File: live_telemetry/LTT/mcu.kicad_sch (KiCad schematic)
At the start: 15 parts, among them J1 Programming Header, U1 MCP2562, U2 PIC18F26K83, Y1 Crystal

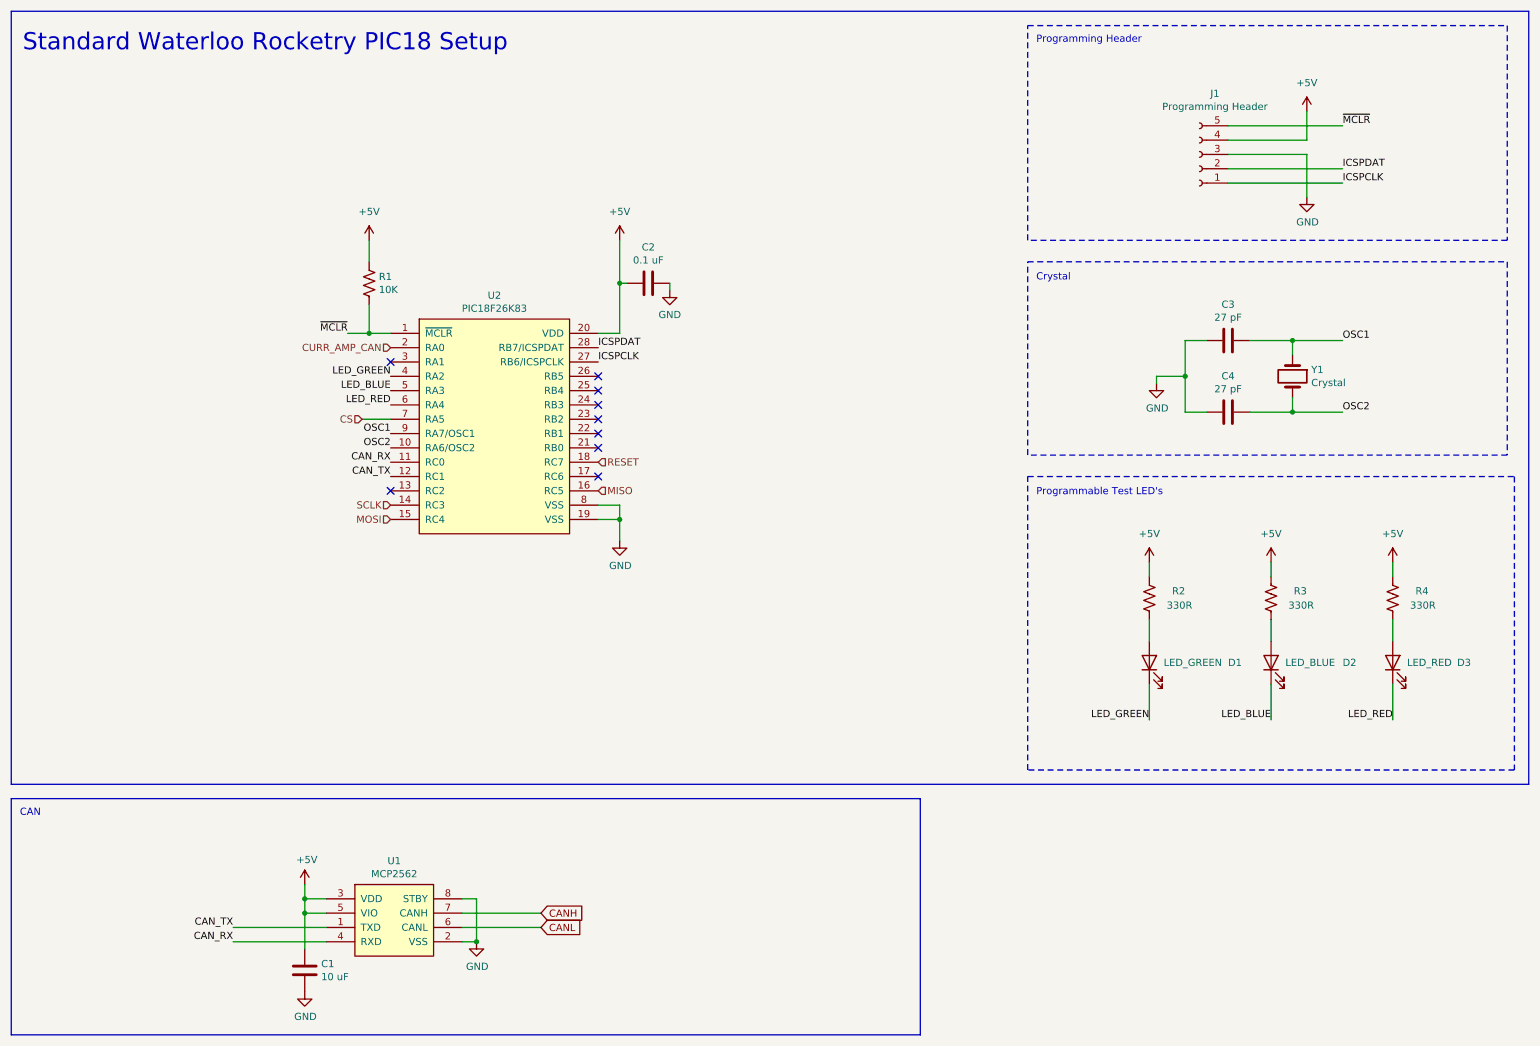
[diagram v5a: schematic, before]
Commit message: changed PIC18 to 3v3 instead of 5v 	- updated current sense ina voltage 	- changed led power connections 	- updated can trx vio
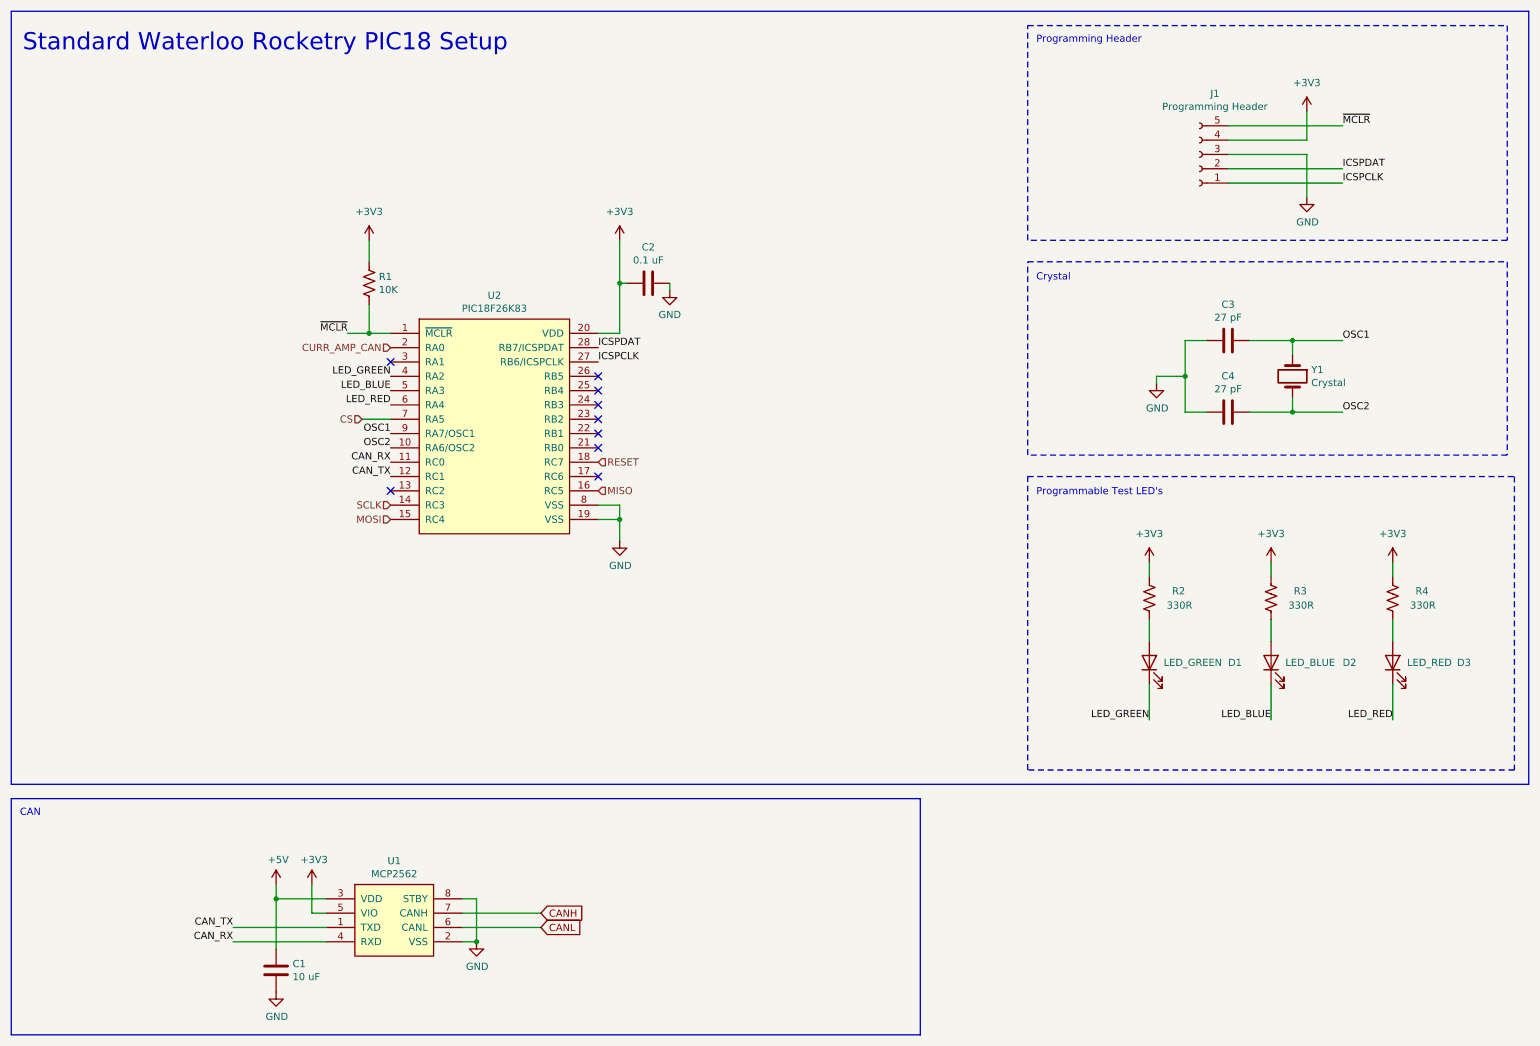
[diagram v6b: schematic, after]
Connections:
- net +5V: no longer C2.2, J1.4 (Pin_4), R1.1, R2.2, R3.2, R4.2, U1.5 (VIO), U2.20 (VDD)
- new net +3V3: C2.2, J1.4 (Pin_4), R1.1, R2.2, R3.2, R4.2, U1.5 (VIO), U2.20 (VDD)
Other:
- moved on the sheet: C1

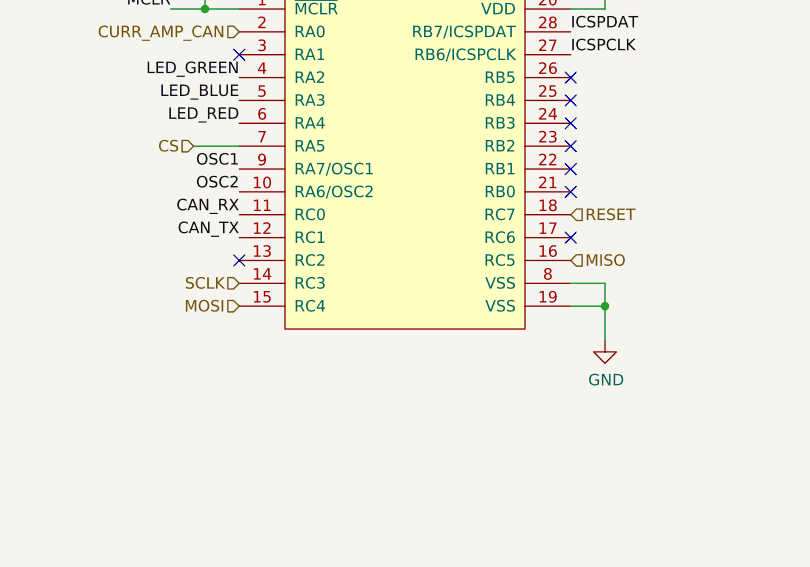
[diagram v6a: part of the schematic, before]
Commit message: swapped mosi/miso lines on pic
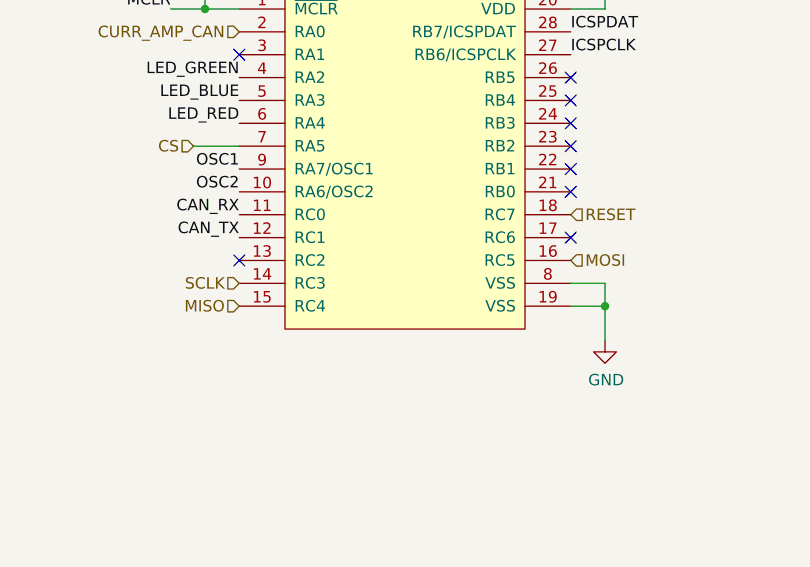
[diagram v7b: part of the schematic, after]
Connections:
- net MISO: now also U2.15 (RC4); no longer U2.16 (RC5)
- net MOSI: now also U2.16 (RC5); no longer U2.15 (RC4)
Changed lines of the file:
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@@
 	(hierarchical_label "MOSI"
+		(shape input)
+		(at 118.11 99.06 0)
+		(effects
+			(font
+				(size 1.27 1.27)
+			)
+			(justify left)
+		)
+	)
+	(hierarchical_label "MISO"
 		(shape input)
 		(at 81.28 104.14 180)
@@
 		)
 	)
-	(hierarchical_label "MISO"
-		(shape input)
-		(at 118.11 99.06 0)
-		(effects
-			(font
-				(size 1.27 1.27)
-			)
-			(justify left)
-		)
-	)
